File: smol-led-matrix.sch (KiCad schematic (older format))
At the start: 1 part

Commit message: Place parts
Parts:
- removed U?: STM32L431CBTx, Package_QFP:LQFP-48_7x7mm_P0.5mm, symbol MCU_ST_STM32L4:STM32L431CBTx
- added C1, C2, C3, C5, C8, C9: 100nF, Capacitor_SMD:C_0402_1005Metric, symbol Device:C
- added C4, C6, C7: 1uF, Capacitor_SMD:C_0402_1005Metric, symbol Device:C
- added D226: 1N4148, Diode_SMD:D_SOD-323F, symbol Device:D
- added D227: LED, LED_SMD:LED_0402_1005Metric, symbol Device:LED
- added J1: USB_C_Receptacle_USB2.0, Connector_USB:USB_C_Receptacle_Palconn_UTC16-G, symbol Connector:USB_C_Receptacle_USB2.0
- added J2: TagConnect_TC2030_SWD, Connector:Tag-Connect_TC2030-IDC-NL_2x03_P1.27mm_Vertical, symbol Connector_TagConnect:TagConnect_TC2030_SWD
- added Q1: FS8205, Package_TO_SOT_SMD:SOT-23-6, symbol Transistor_FET_Dual:FS8205
- added Q2: AO3401A, Package_TO_SOT_SMD:SOT-23, symbol Transistor_FET:AO3401A
- added R1, R2: 5.1kR, Resistor_SMD:R_0402_1005Metric, symbol Device:R
- added R3, R4, R5: 27kR, Resistor_SMD:R_0402_1005Metric, symbol Device:R
- added RN1, RN2, RN3, RN4, RN5: 1kR, Resistor_SMD:R_Array_Concave_4x0402, symbol Device:R_Pack04
- added SW1, SW2: SW_Push, Button_Switch_SMD:SW_Push_SPST_NO_Alps_SKRK, symbol Switch:SW_Push
- added TP1: BAT+, TestPoint:TestPoint_Pad_2.0x2.0mm, symbol Connector:TestPoint
- added TP2: BAT-, TestPoint:TestPoint_Pad_2.0x2.0mm, symbol Connector:TestPoint
- added U1: STM32L433CBTx, Package_QFP:LQFP-48_7x7mm_P0.5mm, symbol MCU_ST_STM32L4:STM32L433CBTx
- added U2: DW01+G, Package_TO_SOT_SMD:SOT-23-6, symbol Battery_Management:AP9101CK6
- added U3: TP4054, Package_TO_SOT_SMD:TSOT-23-5, symbol Battery_Management:LTC4054ES5-4.2
- added U4: XC6206P332MR, Package_TO_SOT_SMD:SOT-23, symbol Regulator_Linear:XC6206PxxxMR
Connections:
- net A0: now also RN1.5 (R4.2)
- net A1: now also RN1.6 (R3.2)
- net A10: now also RN4.6 (R3.2)
- net A11: now also RN4.5 (R4.2)
- net A12: now also RN5.8 (R1.2)
- net A13: now also RN5.7 (R2.2)
- net A14: now also RN5.6 (R3.2)
- net A2: now also RN1.7 (R2.2)
- net A3: now also RN1.8 (R1.2)
- net A4: now also RN3.8 (R1.2)
- net A5: now also RN3.7 (R2.2)
- net A6: now also RN3.6 (R3.2)
- net A7: now also RN3.5 (R4.2)
- net A8: now also RN4.8 (R1.2)
- net A9: now also RN4.7 (R2.2)
- net K0: now also RN1.4 (R4.1), U1.18 (PB0)
- net K1: now also RN1.3 (R3.1), U1.19 (PB1)
- net K10: now also RN4.3 (R3.1), U1.21 (PB10)
- net K11: now also RN4.4 (R4.1), U1.22 (PB11)
- net K12: now also RN5.1 (R1.1), U1.25 (PB12)
- net K13: now also RN5.2 (R2.1), U1.26 (PB13)
- net K14: now also RN5.3 (R3.1), U1.27 (PB14)
- net K2: now also RN1.2 (R2.1), U1.20 (PB2)
- net K3: now also RN1.1 (R1.1), U1.39 (PB3)
- net K4: now also RN3.1 (R1.1), U1.40 (PB4)
- net K5: now also RN3.2 (R2.1), U1.41 (PB5)
- net K6: now also RN3.3 (R3.1), U1.42 (PB6)
- net K7: now also RN3.4 (R4.1), U1.43 (PB7)
- net K8: now also RN4.1 (R1.1), U1.45 (PB8)
- net K9: now also RN4.2 (R2.1), U1.46 (PB9)
- new net: J2.2 (SWDIO), U1.34 (PA13)
- new net: J2.4 (SWCLK), U1.37 (PA14)
- new net: R5.2, SW1.1, U1.44 (PH3)
- new net: J1.A5 (CC1), R1.2
- new net: J1.B5 (CC2), R2.1
- new net: D227.1 (K), U3.1 (~CHRG)
- new net: R3.1, U3.5 (PROG)
- new net: Q1.6, U2.1 (DO)
- new net: RN2.7 (R2.2), U2.2 (VM)
- new net: Q1.4, U2.3 (CO)
- new net: C3.2, RN2.5 (R4.2), RN2.6 (R3.2), U2.5 (VDD)
- new net: C3.1, Q1.1, TP2.1, U2.6 (VSS)
- new net: Q1.2, Q1.5
- new net: C6.1, D226.1 (K), Q2.2 (S), U4.3 (VI)
- new net +3V3: C1.1, C2.1, C7.2, C8.1, C9.1, J2.1 (VTGT), SW1.2, U1.24 (VDD), U1.36 (VDDUSB), U1.48 (VDD), U1.9 (VDDA), U4.2 (VO)
- new net +5V: C4.2, D226.2 (A), J1.A4 (VBUS), J1.A9 (VBUS), J1.B4 (VBUS), J1.B9 (VBUS), J2.6 (SWO), Q2.1 (G), R4.1, RN2.1 (R1.1), U3.4 (VCC)
- new net +BATT: Q2.3 (D), RN2.3 (R3.1), RN2.4 (R4.1), TP1.1, U3.3 (BAT)
- new net CHG_LED+: D227.2 (A), RN2.8 (R1.2)
- new net D+: J1.A6 (D+), J1.B6 (D+), U1.33 (PA12)
- new net D-: J1.A7 (D-), J1.B7 (D-), U1.32 (PA11)
- new net GND: C1.2, C2.2, C4.1, C5.2, C6.2, C7.1, C8.2, C9.2, J1.A1 (GND), J1.A12 (GND), J1.B1 (GND), J1.B12 (GND), J1.S1 (SHIELD), J2.5 (GND), Q1.3, R1.1, R2.2, R3.2, R4.2, R5.1, RN2.2 (R2.1), SW2.2, U1.23 (VSS), U1.35 (VSS), U1.47 (VSS), U1.8 (VSSA), U3.2 (GND), U4.1 (GND)
- new net K15: U1.28 (PB15)
- new net ~RST: C5.1, J2.3 (~RESET), SW2.1, U1.7 (NRST)
- no-connect marks 0 -> 6
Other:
- note added: "Ichg=37mA"

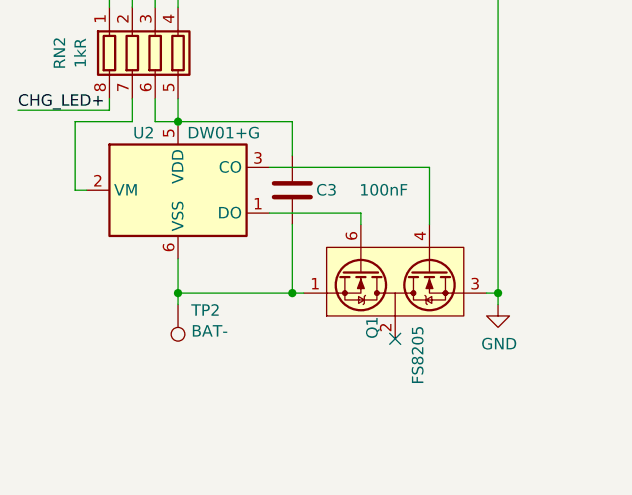
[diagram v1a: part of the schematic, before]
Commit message: Hide designators
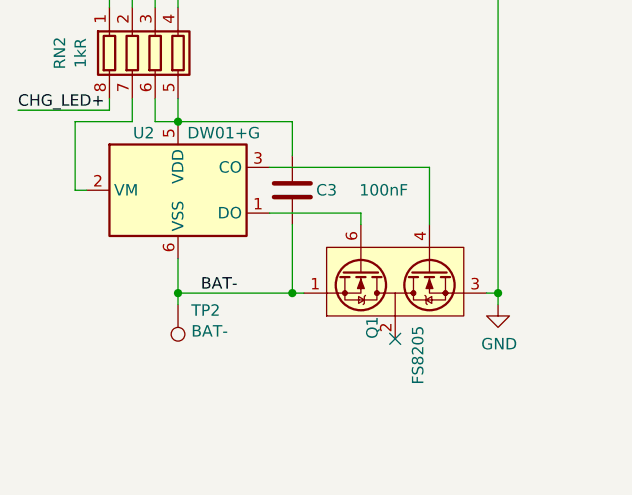
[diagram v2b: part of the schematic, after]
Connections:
- net BAT-: now reaches C3.1, Q1.1, TP2.1, U2.6 (VSS)
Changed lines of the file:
@@
 	1    0    0    1
 $EndComp
+Text Label -3150 6900 0    50   ~ 0
+BAT-
 $EndSCHEMATC

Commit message: Decide BGA ball placement
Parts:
- removed C3: 100nF, Capacitor_SMD:C_0402_1005Metric, symbol Device:C
- removed C4, C6, C7: 1uF, Capacitor_SMD:C_0402_1005Metric, symbol Device:C
- removed D226: 1N4148, Diode_SMD:D_SOD-323F, symbol Device:D
- removed D227: LED, LED_SMD:LED_0402_1005Metric, symbol Device:LED
- removed J1: USB_C_Receptacle_USB2.0, Connector_USB:USB_C_Receptacle_Palconn_UTC16-G, symbol Connector:USB_C_Receptacle_USB2.0
- removed Q1: FS8205, Package_TO_SOT_SMD:SOT-23-6, symbol Transistor_FET_Dual:FS8205
- removed Q2: AO3401A, Package_TO_SOT_SMD:SOT-23, symbol Transistor_FET:AO3401A
- removed R1, R2: 5.1kR, Resistor_SMD:R_0402_1005Metric, symbol Device:R
- removed R3, R4: 27kR, Resistor_SMD:R_0402_1005Metric, symbol Device:R
- removed RN2: 1kR, Resistor_SMD:R_Array_Concave_4x0402, symbol Device:R_Pack04
- removed TP1: BAT+, TestPoint:TestPoint_Pad_2.0x2.0mm, symbol Connector:TestPoint
- removed TP2: BAT-, TestPoint:TestPoint_Pad_2.0x2.0mm, symbol Connector:TestPoint
- removed U2: DW01+G, Package_TO_SOT_SMD:SOT-23-6, symbol Battery_Management:AP9101CK6
- removed U3: TP4054, Package_TO_SOT_SMD:TSOT-23-5, symbol Battery_Management:LTC4054ES5-4.2
- removed U4: XC6206P332MR, Package_TO_SOT_SMD:SOT-23, symbol Regulator_Linear:XC6206PxxxMR
- added TP? (x62): TestPoint, TestPoint:TestPoint_Pad_D1.0mm, symbol Connector:TestPoint
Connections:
- net A0: now also TP?.1, TP?.1
- net A1: now also TP?.1, TP?.1
- net A10: now also RN4.5 (R4.2), TP?.1, TP?.1; no longer RN4.6 (R3.2)
- net A11: now also RN4.6 (R3.2), TP?.1, TP?.1; no longer RN4.5 (R4.2)
- net A12: now also TP?.1, TP?.1
- net A13: now also TP?.1, TP?.1
- net A14: now also TP?.1, TP?.1
- net A2: now also TP?.1, TP?.1
- net A3: now also TP?.1, TP?.1
- net A4: now also TP?.1, TP?.1
- net A5: now also TP?.1, TP?.1
- net A6: now also TP?.1, TP?.1
- net A7: now also TP?.1, TP?.1
- net A8: now also TP?.1, TP?.1
- net A9: now also TP?.1, TP?.1
- net K0: now also TP?.1, TP?.1
- net K1: now also TP?.1, TP?.1
- net K10: now also RN4.4 (R4.1), TP?.1, TP?.1; no longer RN4.3 (R3.1)
- net K11: now also RN4.3 (R3.1), TP?.1, TP?.1; no longer RN4.4 (R4.1)
- net K12: now also TP?.1, TP?.1
- net K13: now also TP?.1, TP?.1
- net K14: now also TP?.1, TP?.1
- net K15: now also TP?.1, TP?.1
- net K2: now also TP?.1, TP?.1
- net K3: now also TP?.1, TP?.1
- net K4: now also TP?.1, TP?.1
- net K5: now also TP?.1, TP?.1
- net K6: now also TP?.1, TP?.1
- net K7: now also TP?.1, TP?.1
- net K8: now also TP?.1, TP?.1
- net K9: now also TP?.1, TP?.1
- no-connect marks 6 -> 3
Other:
- note removed: "Ichg=37mA"
- moved on the sheet: C1, C2, C5, C8, C9, J2, R5, RN1, RN3, RN4, RN5, SW1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

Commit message: Layout half done
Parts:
- gave numbers to parts that had none: 62
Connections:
- net A12: now also RN5.5 (R4.2); no longer RN5.8 (R1.2)
- net A13: now also RN5.6 (R3.2); no longer RN5.7 (R2.2)
- net A14: now also RN5.7 (R2.2); no longer RN5.6 (R3.2)
- net A15: now also RN5.8 (R1.2), TP33.1, TP64.1
- net K12: now also RN5.4 (R4.1); no longer RN5.1 (R1.1)
- net K13: now also RN5.3 (R3.1); no longer RN5.2 (R2.1)
- net K14: now also RN5.2 (R2.1); no longer RN5.3 (R3.1)
- net K15: now also RN5.1 (R1.1); no longer TP33.1, TP64.1
- no-connect marks 3 -> 1
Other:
- moved on the sheet: TP33, TP49, TP50, TP51, TP52, TP53, TP54, TP55, TP56, TP57, TP58, TP59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

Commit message: Finish control board layout
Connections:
- net BOOT0: now reaches R5.2, SW1.1, U1.44 (PH3)
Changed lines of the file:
@@
 Wire Wire Line
 	1200 7200 1000 7200
+Text Label 1050 5100 0    50   ~ 0
+BOOT0
 $EndSCHEMATC

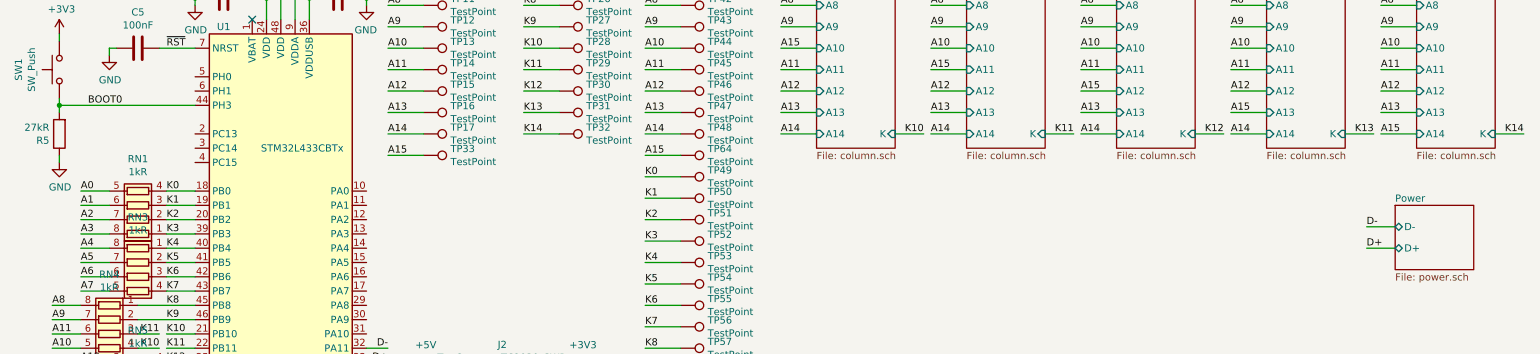
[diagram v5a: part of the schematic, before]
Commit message: Add charge current monitoring
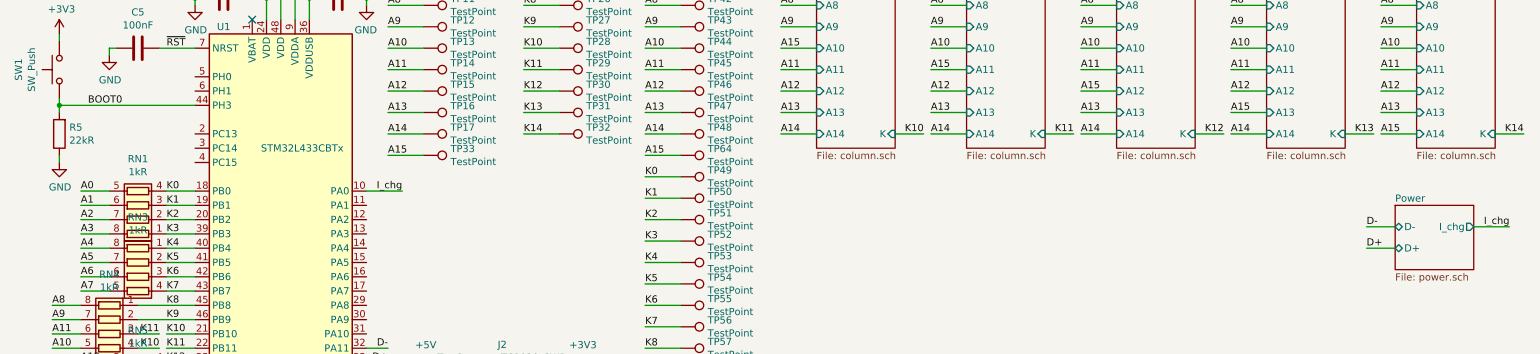
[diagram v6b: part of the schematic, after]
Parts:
- R5: value 27kR -> 22kR; LCSC C25771 -> C25768
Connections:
- net I_chg: now reaches U1.10 (PA0)
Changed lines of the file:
@@
 	0    1    1    0
-$EndComp
-$Comp
-L Device:R R5
-U 1 1 63080375
-P 850 5300
-F 0 "R5" H 920 5346 50  0000 L CNN
-F 1 "27kR" H 920 5255 50  0000 L CNN
-F 2 "Resistor_SMD:R_0402_1005Metric" V 780 5300 50  0001 C CNN
-F 3 "~" H 850 5300 50  0001 C CNN
-F 4 "C25771" V 850 5300 50  0001 C CNN "LCSC"
-	1    850  5300
-	-1   0    0    1
 $EndComp
 Wire Wire Line
@@
 F2 "D-" B L 10200 5950 50
 F3 "D+" B L 10200 6100 50
+F4 "I_chg" O R 10750 5950 50
 $EndSheet
 Wire Wire Line
@@
 Text Label 1050 5100 0    50   ~ 0
 BOOT0
+Text Label 11000 5950 2    50   ~ 0
+I_chg
+Wire Wire Line
+	10750 5950 11000 5950
+Text Label 3250 5700 2    50   ~ 0
+I_chg
+Wire Wire Line
+	3000 5700 3250 5700
+$Comp
+L Device:R R5
+U 1 1 63080375
+P 850 5300
+F 0 "R5" H 780 5254 50  0000 R CNN
+F 1 "22kR" H 780 5345 50  0000 R CNN
+F 2 "Resistor_SMD:R_0402_1005Metric" V 780 5300 50  0001 C CNN
+F 3 "~" H 850 5300 50  0001 C CNN
+F 4 "C25768" V 850 5300 50  0001 C CNN "LCSC"
+	1    850  5300
+	-1   0    0    1
+$EndComp
 $EndSCHEMATC

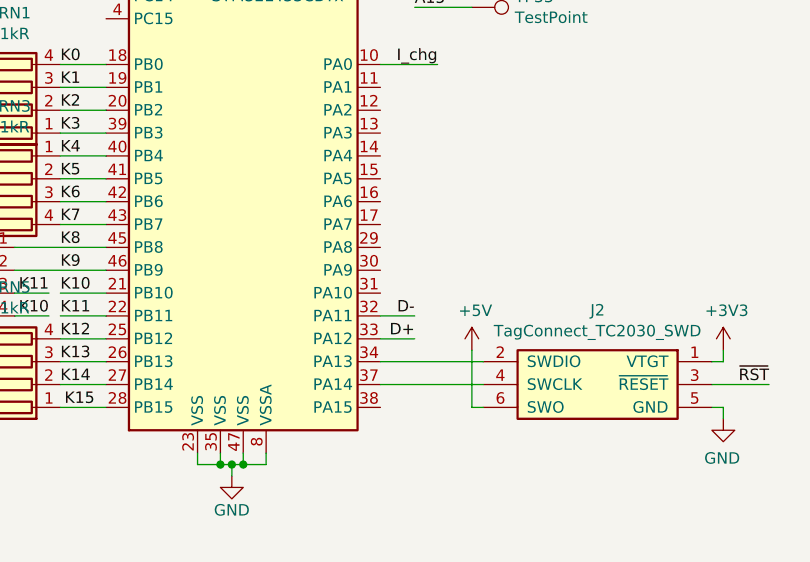
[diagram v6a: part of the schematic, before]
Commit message: Break out BOOT0 to additional GPIO
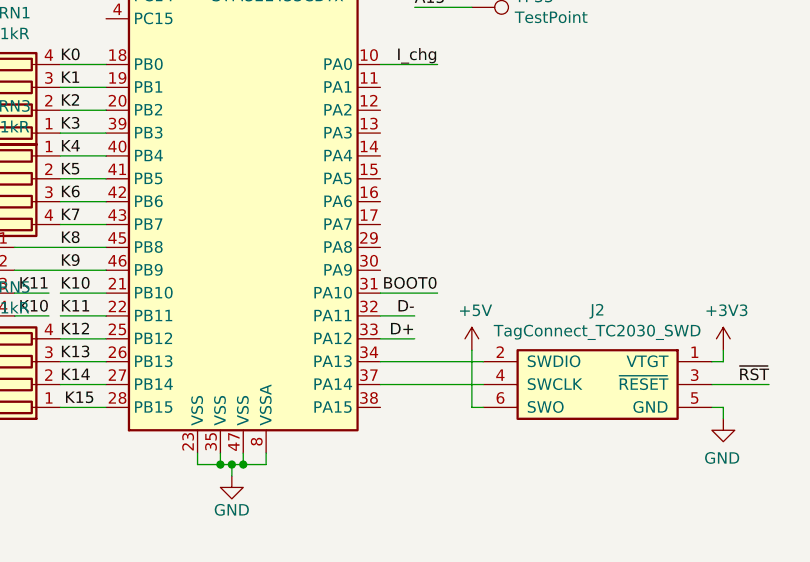
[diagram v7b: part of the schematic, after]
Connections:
- net BOOT0: now also U1.31 (PA10)
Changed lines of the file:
@@
 	-1   0    0    1
 $EndComp
+Wire Wire Line
+	3000 6700 3250 6700
+Text Label 3250 6700 2    50   ~ 0
+BOOT0
 $EndSCHEMATC
